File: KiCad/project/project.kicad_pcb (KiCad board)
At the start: 2 copper layers, 161 x 95.5 mm, 11 parts, among them U1 NUCLEO-L476RG

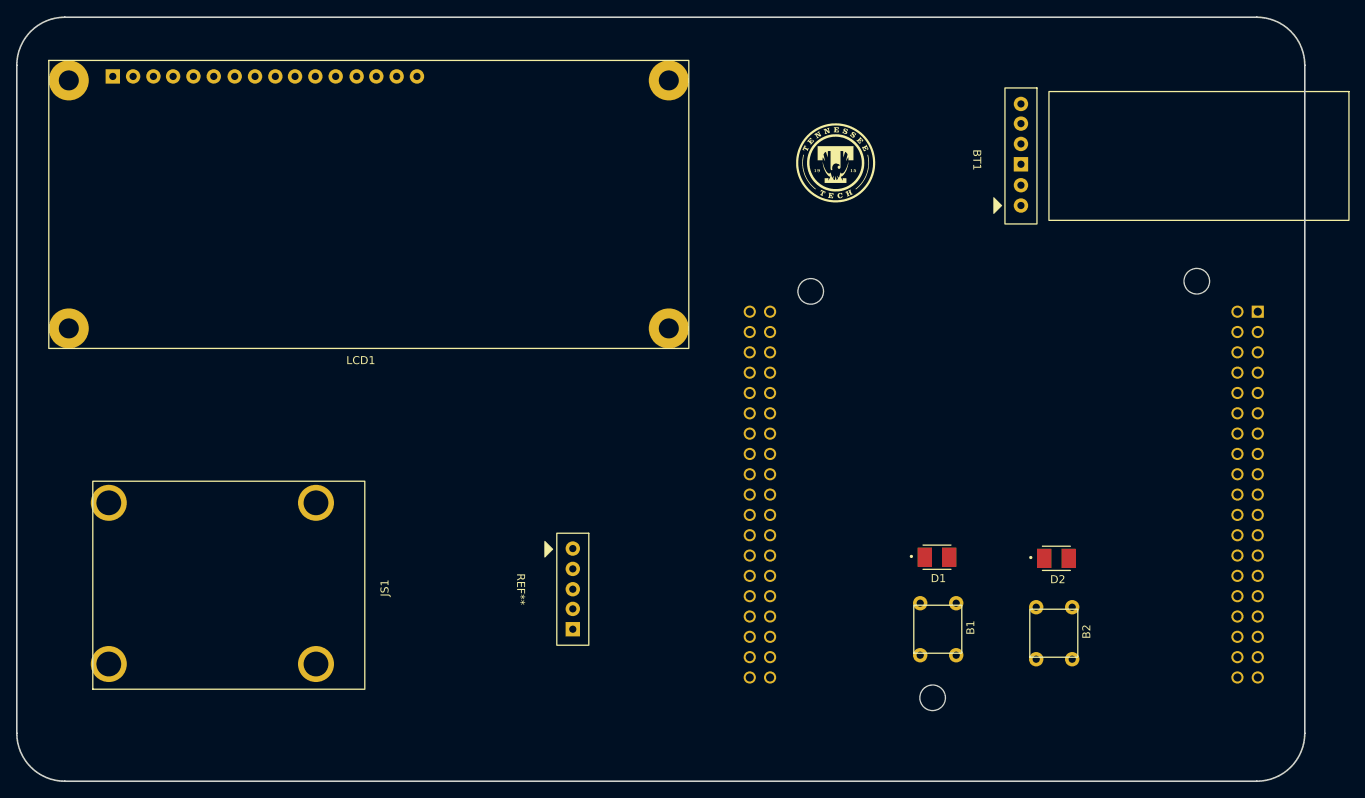
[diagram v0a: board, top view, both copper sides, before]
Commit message: Updated PCB schematic and pinout for the ioc file because it was funky
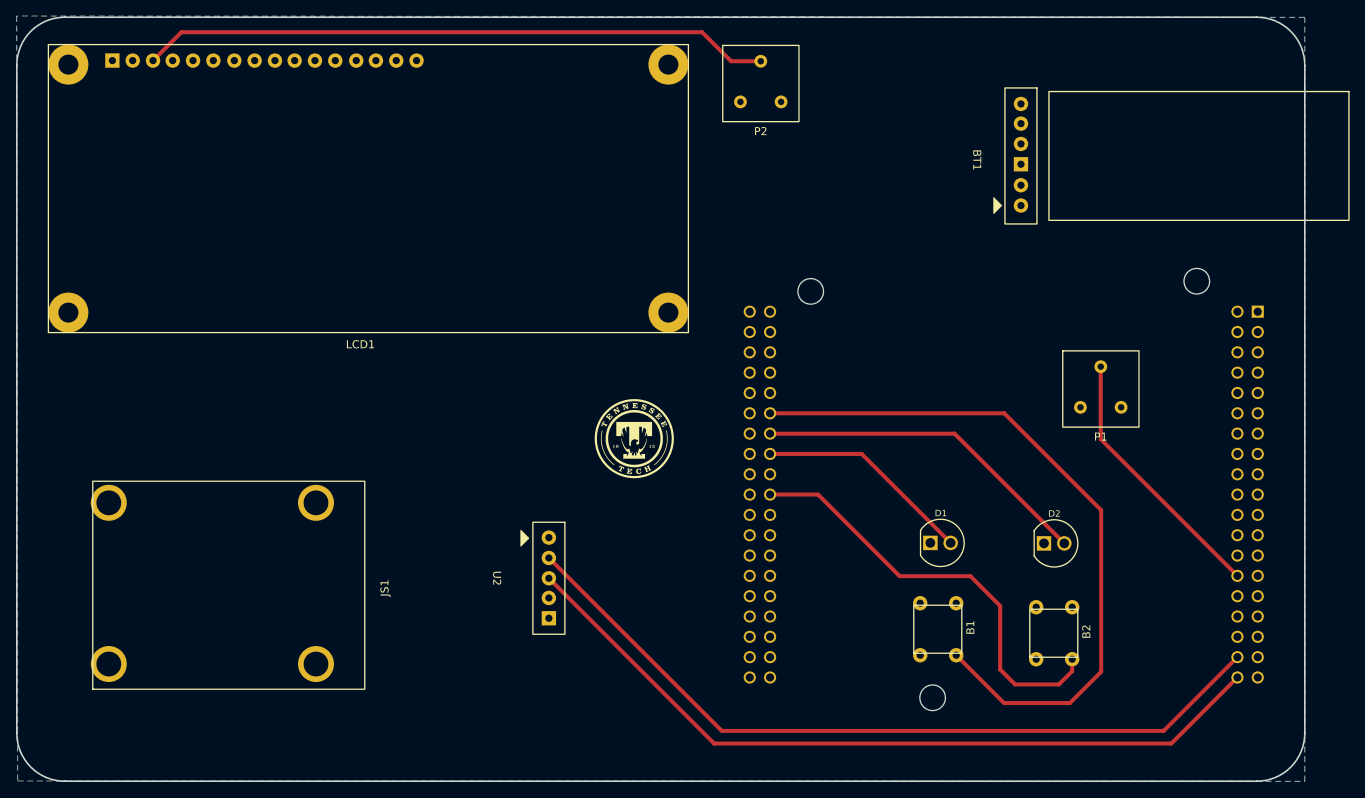
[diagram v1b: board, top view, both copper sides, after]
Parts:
- removed REF**: Joystick_Pins, Embedded_Footprints:Joystick_Pins
- added P1: ~, Embedded_Footprints:Potentiometer, F.Cu at (189.0, 114.5)
- added P2: ~, Embedded_Footprints:Potentiometer, F.Cu at (146.5, 76.3)
- added U2: ~, Embedded_Footprints:Joystick_Pins, F.Cu at (113.0, 131.6)
- D1, D2: footprint Embedded_Footprints:LED -> Embedded_Footprints:LED_THRU
- moved G*** 42.7 mm to (130.7, 114.2)
- moved D2 5.04 mm to (183.2, 127.3)
- moved D1 4.95 mm to (169.0, 127.2)
- moved LCD1 1.98 mm to (96.5, 102.9)
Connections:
- B1 pad 1: unconnected-(B1-Pad1) -> +5V
- B1 pad 2: unconnected-(B1-Pad2) -> /SD_BTN
- B1 pad 4: Net-(D1-A) -> Net-(B1-Pad4)
- B2 pad 1: unconnected-(B2-Pad1) -> +5V
- B2 pad 2: unconnected-(B2-Pad2) -> /MM_BTN
- B2 pad 4: Net-(D2-A) -> Net-(B2-Pad4)
- BT1 pad 1: unconnected-(BT1-EN-Pad1) -> /BT_EN
- BT1 pad 2: unconnected-(BT1-Vcc-Pad2) -> +5V
- BT1 pad 3: unconnected-(BT1-GND-Pad3) -> GND
- BT1 pad 4: unconnected-(BT1-TX-Pad4) -> /BT_TX
- BT1 pad 5: unconnected-(BT1-RX-Pad5) -> /BT_RX
- BT1 pad 6: unconnected-(BT1-State-Pad6) -> /BT_ST
- D1 pad 2: Net-(D1-A) -> /SD_LED
- D2 pad 2: Net-(D2-A) -> /MM_LED
- LCD1 pad 1: unconnected-(LCD1-GND-Pad1) -> GND
- LCD1 pad 10: unconnected-(LCD1-Data3-Pad10) -> /LCD_D3
- LCD1 pad 11: unconnected-(LCD1-Data4-Pad11) -> /LCD_D4
- LCD1 pad 12: unconnected-(LCD1-Data5-Pad12) -> /LCD_D5
- LCD1 pad 13: unconnected-(LCD1-Data6-Pad13) -> /LCD_D6
- LCD1 pad 14: unconnected-(LCD1-Data7-Pad14) -> /LCD_D7
- LCD1 pad 15: (no net) -> +5V
- LCD1 pad 16: (no net) -> GND
- LCD1 pad 2: unconnected-(LCD1-Vcc-Pad2) -> +5V
- LCD1 pad 3: unconnected-(LCD1-VE-Pad3) -> /LCD_Pot
- LCD1 pad 4: unconnected-(LCD1-RS-Pad4) -> /LCD_RS
- LCD1 pad 5: unconnected-(LCD1-R/W-Pad5) -> GND
- LCD1 pad 6: unconnected-(LCD1-EN-Pad6) -> /LCD_EN
- LCD1 pad 7: unconnected-(LCD1-Data0-Pad7) -> /LCD_D0
- LCD1 pad 8: unconnected-(LCD1-Data1-Pad8) -> /LCD_D1
- LCD1 pad 9: unconnected-(LCD1-Data2-Pad9) -> /LCD_D2
- U1 pad CN10_11: unconnected-(U1B-PA5-PadCN10_11) -> /SD_BTN
- U1 pad CN10_12: unconnected-(U1B-PA12-PadCN10_12) -> /LCD_D4
- U1 pad CN10_13: unconnected-(U1B-PA6-PadCN10_13) -> /MM_LED
- U1 pad CN10_14: unconnected-(U1B-PA11-PadCN10_14) -> /LCD_D5
- U1 pad CN10_15: unconnected-(U1B-PA7-PadCN10_15) -> /SD_LED
- U1 pad CN10_16: unconnected-(U1B-PB12-PadCN10_16) -> /LCD_D2
- U1 pad CN10_18: unconnected-(U1B-PB11-PadCN10_18) -> /LCD_D3
- U1 pad CN10_19: unconnected-(U1B-PC7-PadCN10_19) -> /MM_BTN
- U1 pad CN10_2: unconnected-(U1B-PC8-PadCN10_2) -> /LCD_D0
- U1 pad CN10_22: unconnected-(U1B-PB2-PadCN10_22) -> /LCD_D6
- U1 pad CN10_24: unconnected-(U1B-PB1-PadCN10_24) -> /LCD_D7
- U1 pad CN10_32: unconnected-(U1B-AGND-PadCN10_32) -> GND
- U1 pad CN10_35: unconnected-(U1B-PA2-PadCN10_35) -> /BT_TX
- U1 pad CN10_37: unconnected-(U1B-PA3-PadCN10_37) -> /BT_RX
- U1 pad CN10_4: unconnected-(U1B-PC6-PadCN10_4) -> /LCD_D1
- U1 pad CN10_9: unconnected-(U1B-GND_CN10_9-PadCN10_9) -> GND
- U1 pad CN7_1: unconnected-(U1A-PC10-PadCN7_1) -> /LCD_RS
- U1 pad CN7_16: unconnected-(U1A-+3V3-PadCN7_16) -> +3.3V
- U1 pad CN7_18: unconnected-(U1A-+5V-PadCN7_18) -> +5V
- U1 pad CN7_19: unconnected-(U1A-GND_CN7_19-PadCN7_19) -> GND
- U1 pad CN7_20: unconnected-(U1A-GND_CN7_20-PadCN7_20) -> GND
- U1 pad CN7_22: unconnected-(U1A-GND_CN7_22-PadCN7_22) -> GND
- U1 pad CN7_28: unconnected-(U1A-PA0-PadCN7_28) -> /Pot_Val
- U1 pad CN7_3: unconnected-(U1A-PC12-PadCN7_3) -> /LCD_EN
- U1 pad CN7_35: unconnected-(U1A-PC2-PadCN7_35) -> /BT_ST
- U1 pad CN7_36: unconnected-(U1A-PC1-PadCN7_36) -> /JS_Y
- U1 pad CN7_37: unconnected-(U1A-PC3-PadCN7_37) -> /BT_EN
- U1 pad CN7_38: unconnected-(U1A-PC0-PadCN7_38) -> /JS_X
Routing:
- net /JS_Y: track 0.00 -> 98.8 mm
- net /JS_X: track 0.00 -> 98.0 mm
- net /SD_BTN: track 0.00 -> 88.8 mm
- net /LCD_Pot: track 0.00 -> 78.9 mm
- net /MM_BTN: track 0.00 -> 54.4 mm
- net /MM_LED: track 0.00 -> 42.5 mm
- net /Pot_Val: track 0.00 -> 33.2 mm
- net /SD_LED: track 0.00 -> 27.2 mm
- added copper zone on B.Cu, net GND

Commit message: Update stuff :)
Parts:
- added H1: ~, Embedded_Footprints:OLED, F.Cu at (118.2, 107.2)
- added R1: R_US, Embedded_Footprints:RESC3216X65, F.Cu at (176.4, 138.2)
- added R2: R_US, Embedded_Footprints:RESC3216X65, F.Cu at (191.0, 138.1)
- moved G*** 41.9 mm to (170.6, 101.3)
- moved U2 37.5 mm to (77.4, 143.5), turned to 180 degrees
- moved JS1 25.6 mm to (77.2, 144.5), turned to 0 degrees
- moved B2 5.51 mm to (183.5, 141.9), turned to 0 degrees
- moved B1 5.37 mm to (169.8, 141.9), turned to 0 degrees
- moved D1 0.88 mm to (169.8, 127.0)
- moved D2 0.64 mm to (183.7, 127.0)
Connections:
- U1 pad CN10_11: /SD_BTN -> unconnected-(U1B-PA5-PadCN10_11)
- U1 pad CN10_14: /LCD_D5 -> /LCD_D3
- U1 pad CN10_17: unconnected-(U1B-PB6-PadCN10_17) -> /SD_BTN
- U1 pad CN10_18: /LCD_D3 -> /LCD_D1
- U1 pad CN10_2: /LCD_D0 -> /LCD_D7
- U1 pad CN10_22: /LCD_D6 -> /LCD_D0
- U1 pad CN10_24: /LCD_D7 -> /LCD_EN
- U1 pad CN10_26: unconnected-(U1B-PB15-PadCN10_26) -> /LCD_RS
- U1 pad CN10_28: unconnected-(U1B-PB14-PadCN10_28) -> /OLED_SDA
- U1 pad CN10_3: unconnected-(U1B-PB8-PadCN10_3) -> /BT_ST
- U1 pad CN10_30: unconnected-(U1B-PB13-PadCN10_30) -> /OLED_SCL
- U1 pad CN10_32: GND -> unconnected-(U1B-AGND-PadCN10_32)
- U1 pad CN10_35: /BT_TX -> unconnected-(U1B-PA2-PadCN10_35)
- U1 pad CN10_37: /BT_RX -> unconnected-(U1B-PA3-PadCN10_37)
- U1 pad CN10_4: /LCD_D1 -> /LCD_D6
- U1 pad CN10_5: unconnected-(U1B-PB9-PadCN10_5) -> /BT_EN
- U1 pad CN10_6: unconnected-(U1B-PC5-PadCN10_6) -> /LCD_D5
- U1 pad CN7_1: /LCD_RS -> unconnected-(U1A-PC10-PadCN7_1)
- U1 pad CN7_3: /LCD_EN -> /BT_TX
- U1 pad CN7_35: /BT_ST -> unconnected-(U1A-PC2-PadCN7_35)
- U1 pad CN7_37: /BT_EN -> unconnected-(U1A-PC3-PadCN7_37)
- U1 pad CN7_4: unconnected-(U1A-PD2-PadCN7_4) -> /BT_RX
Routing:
- net +5V: track 0.05 -> 385.4 mm
- net +3.3V: track 0.00 -> 119.6 mm, vias 0 -> 2
- net /LCD_RS: track 0.00 -> 97.8 mm
- net /LCD_EN: track 0.00 -> 92.9 mm
- net /LCD_D0: track 0.00 -> 89.3 mm
- net /LCD_D1: track 0.00 -> 84.7 mm
- net /LCD_D2: track 0.00 -> 81.1 mm
- net /LCD_D3: track 0.00 -> 76.2 mm
- net /LCD_D4: track 0.00 -> 72.6 mm
- net /LCD_D5: track 0.00 -> 66.9 mm
- net /LCD_D6: track 0.00 -> 63.2 mm
- net /BT_TX: track 0.00 -> 59.7 mm
- net /LCD_D7: track 0.00 -> 59.7 mm
- net /SD_BTN: track 88.8 -> 31.1 mm
- net /BT_RX: track 0.00 -> 55.5 mm
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
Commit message: Updated schematic to get ready to send out
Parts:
- moved G*** 1.01 mm to (61.7, 150.0)
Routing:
- net +5V: track 385.4 -> 412.4 mm
- net /Pot_Val: track 36.5 -> 35.0 mm
- net /BT_TX: track 59.7 -> 60.9 mm
- net +3.3V: track 119.6 -> 120.1 mm, vias 2 -> 1
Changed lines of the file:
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@@
 	(footprint "Graphics:TA_Logo"
 		(layer "B.Cu")
-		(at 61.91 151.01 180)
+		(at 61.7 150.02 180)
 		(property "Reference" "G***"
 			(at 0 0 180)
@@
 	)
 	(segment
+		(start 202.98 121.73)
+		(end 202.98 145.82)
+		(width 0.5)
+		(layer "F.Cu")
+		(net 2)
+	)
+	(segment
+		(start 76.88 153.6)
+		(end 74.94 151.66)
+		(width 0.5)
+		(layer "F.Cu")
+		(net 2)
+	)
+	(segment
 		(start 179.36 68.17)
 		(end 152.94951 68.17)
@@
 	)
 	(segment
-		(start 77.01 153.73)
-		(end 73.86 150.58)
-		(width 0.5)
-		(layer "F.Cu")
-		(net 2)
-	)
-	(segment
 		(start 149.037353 72.082157)
 		(end 147.267843 72.082157)
@@
 	)
 	(segment
+		(start 206.08 118.63)
+		(end 195.58 118.63)
+		(width 0.5)
+		(layer "F.Cu")
+		(net 2)
+	)
+	(segment
 		(start 152.94951 68.17)
 		(end 149.037353 72.082157)
@@
 	)
 	(segment
+		(start 74.94 151.66)
+		(end 74.94 150.48)
+		(width 0.5)
+		(layer "F.Cu")
+		(net 2)
+	)
+	(segment
 		(start 166.34 135.125)
 		(end 169.285 132.18)
@@
 	)
 	(segment
-		(start 202.39 146.41)
-		(end 195.07 153.73)
-		(width 0.5)
-		(layer "F.Cu")
-		(net 2)
-	)
-	(segment
 		(start 104.33 70.32)
 		(end 100.93 66.92)
@@
 	)
 	(segment
-		(start 200.12 118.63)
-		(end 191.537353 127.212647)
+		(start 202.98 145.82)
+		(end 195.2 153.6)
 		(width 0.5)
 		(layer "F.Cu")
@@
 	)
 	(segment
+		(start 195.58 118.63)
+		(end 191.537353 122.672647)
+		(width 0.5)
+		(layer "F.Cu")
+		(net 2)
+	)
+	(segment
+		(start 206.08 118.63)
+		(end 202.98 121.73)
+		(width 0.5)
+		(layer "F.Cu")
+		(net 2)
+	)
+	(segment
 		(start 191.537353 110.262157)
 		(end 191.537353 127.212647)
@@
 	)
 	(segment
-		(start 206.08 118.63)
-		(end 200.12 118.63)
-		(width 0.5)
-		(layer "F.Cu")
-		(net 2)
-	)
-	(segment
 		(start 191.537353 110.262157)
 		(end 191.537353 90.057353)
@@
 	)
 	(segment
-		(start 195.07 153.73)
-		(end 77.01 153.73)
+		(start 195.2 153.6)
+		(end 76.88 153.6)
 		(width 0.5)
 		(layer "F.Cu")
@@
 	)
 	(segment
+		(start 177.48 90.88)
+		(end 174.19 87.59)
+		(width 0.5)
+		(layer "B.Cu")
+		(net 9)
+	)
+	(segment
+		(start 208.47 90.88)
+		(end 177.48 90.88)
+		(width 0.5)
+		(layer "B.Cu")
+		(net 9)
+	)
+	(segment
 		(start 174.19 82.17)
 		(end 179.02 77.34)
@@
 	)
 	(segment
-		(start 211.49 96.64)
-		(end 205.73 90.88)
+		(start 211 100.26)
+		(end 211 93.41)
 		(width 0.5)
 		(layer "B.Cu")
@@
 	)
 	(segment
-		(start 211.49 99.77)
-		(end 211.49 96.64)
+		(start 211 93.41)
+		(end 208.47 90.88)
 		(width 0.5)
 		(layer "B.Cu")
@@
 	)
 	(segment
-		(start 177.48 90.88)
-		(end 174.19 87.59)
+		(start 208.62 100.85)
+		(end 210.41 100.85)
 		(width 0.5)
 		(layer "B.Cu")
@@
 	)
 	(segment
-		(start 205.73 90.88)
-		(end 177.48 90.88)
+		(start 210.41 100.85)
+		(end 211 100.26)
 		(width 0.5)
 		(layer "B.Cu")
@@
 		(start 174.19 87.59)
 		(end 174.19 82.17)
-		(width 0.5)
-		(layer "B.Cu")
-		(net 9)
-	)
-	(segment
-		(start 210.41 100.85)
-		(end 211.49 99.77)
-		(width 0.5)
-		(layer "B.Cu")
-		(net 9)
-	)
-	(segment
-		(start 208.62 100.85)
-		(end 210.41 100.85)
 		(width 0.5)
 		(layer "B.Cu")
@@
 	)
 	(segment
-		(start 202.71 122.25)
-		(end 202.71 135.4)
+		(start 186.21 151.9)
+		(end 136.53 151.9)
 		(width 0.5)
 		(layer "F.Cu")
@@
 	)
 	(segment
-		(start 136.59 151.96)
+		(start 200.22 137.89)
+		(end 186.21 151.9)
+		(width 0.5)
+		(layer "F.Cu")
+		(net 24)
+	)
+	(segment
+		(start 136.53 151.9)
 		(end 119.43 134.8)
 		(width 0.5)
@@
 	)
 	(segment
-		(start 202.71 116.62)
-		(end 202.71 116.64)
+		(start 200.22 121.91)
+		(end 200.22 137.89)
 		(width 0.5)
 		(layer "F.Cu")
 		(net 24)
 	)
-	(segment
-		(start 203.24 116.09)
-		(end 202.71 116.62)
-		(width 0.5)
-		(layer "F.Cu")
-		(net 24)
-	)
-	(segment
-		(start 202.71 135.4)
-		(end 186.15 151.96)
-		(width 0.5)
-		(layer "F.Cu")
-		(net 24)
-	)
-	(segment
-		(start 203.24 116.09)
-		(end 206.08 116.09)
-		(width 0.5)
-		(layer "F.Cu")
-		(net 24)
-	)
-	(segment
-		(start 186.15 151.96)
-		(end 136.59 151.96)
-		(width 0.5)
-		(layer "F.Cu")
-		(net 24)
-	)
 	(via
-		(at 202.71 122.25)
+		(at 200.22 121.91)
 		(size 0.6)
 		(drill 0.3)
@@
 		(net 24)
 	)
-	(via
-		(at 202.71 116.64)
-		(size 0.6)
-		(drill 0.3)
-		(layers "F.Cu" "B.Cu")
+	(segment
+		(start 202.33 116.09)
+		(end 206.08 116.09)
+		(width 0.5)
+		(layer "B.Cu")
 		(net 24)
 	)
 	(segment
-		(start 202.71 116.64)
-		(end 202.71 122.25)
+		(start 200.22 118.2)
+		(end 202.33 116.09)
 		(width 0.5)
 		(layer "B.Cu")
@@
 	)
 	(segment
-		(start 78.86 150.58)
+		(start 200.22 121.91)
+		(end 200.22 118.2)
+		(width 0.5)
+		(layer "B.Cu")
+		(net 24)
+	)
+	(segment
+		(start 79.94 151.66)
 		(end 81.1 152.82)
+		(width 0.5)
+		(layer "B.Cu")
+		(net 25)
+	)
+	(segment
+		(start 194.75 152.82)
+		(end 206.08 141.49)
 		(width 0.5)
 		(layer "B.Cu")
@@
 	)
 	(segment
-		(start 194.75 152.82)
-		(end 206.08 141.49)
+		(start 79.94 150.48)
+		(end 79.94 151.66)
 		(width 0.5)
 		(layer "B.Cu")
@@
 	)
 	(segment
-		(start 80.23 154.49)
-		(end 76.32 150.58)
+		(start 195.62 154.49)
+		(end 80.23 154.49)
 		(width 0.5)
 		(layer "B.Cu")
@@
 	)
 	(segment
-		(start 195.62 154.49)
-		(end 80.23 154.49)
+		(start 77.4 151.66)
+		(end 77.4 150.48)
 		(width 0.5)
 		(layer "B.Cu")
@@
 	)
 	(segment
-		(start 199.42 110)
-		(end 194.602157 105.182157)
+		(start 80.23 154.49)
+		(end 77.4 151.66)
+		(width 0.5)
+		(layer "B.Cu")
+		(net 26)
+	)
+	(segment
+		(start 206.08 131.33)
+		(end 195.35 120.6)
 		(width 0.5)
 		(layer "B.Cu")
@@
 	)
 	(segment
-		(start 199.42 124.67)
-		(end 199.42 110)
+		(start 195.35 108.47)
+		(end 192.062157 105.182157)
 		(width 0.5)
 		(layer "B.Cu")
@@
 	)
 	(segment
-		(start 206.08 131.33)
-		(end 199.42 124.67)
+		(start 192.062157 105.182157)
+		(end 188.997353 105.182157)
 		(width 0.5)
 		(layer "B.Cu")
@@
 	)
 	(segment
-		(start 194.602157 105.182157)
-		(end 188.997353 105.182157)
-		(width 0.5)
-		(layer "B.Cu")
+		(start 195.35 120.6)
+		(end 195.35 108.47)
+		(width 0.5)
+		(layer "B.Cu")

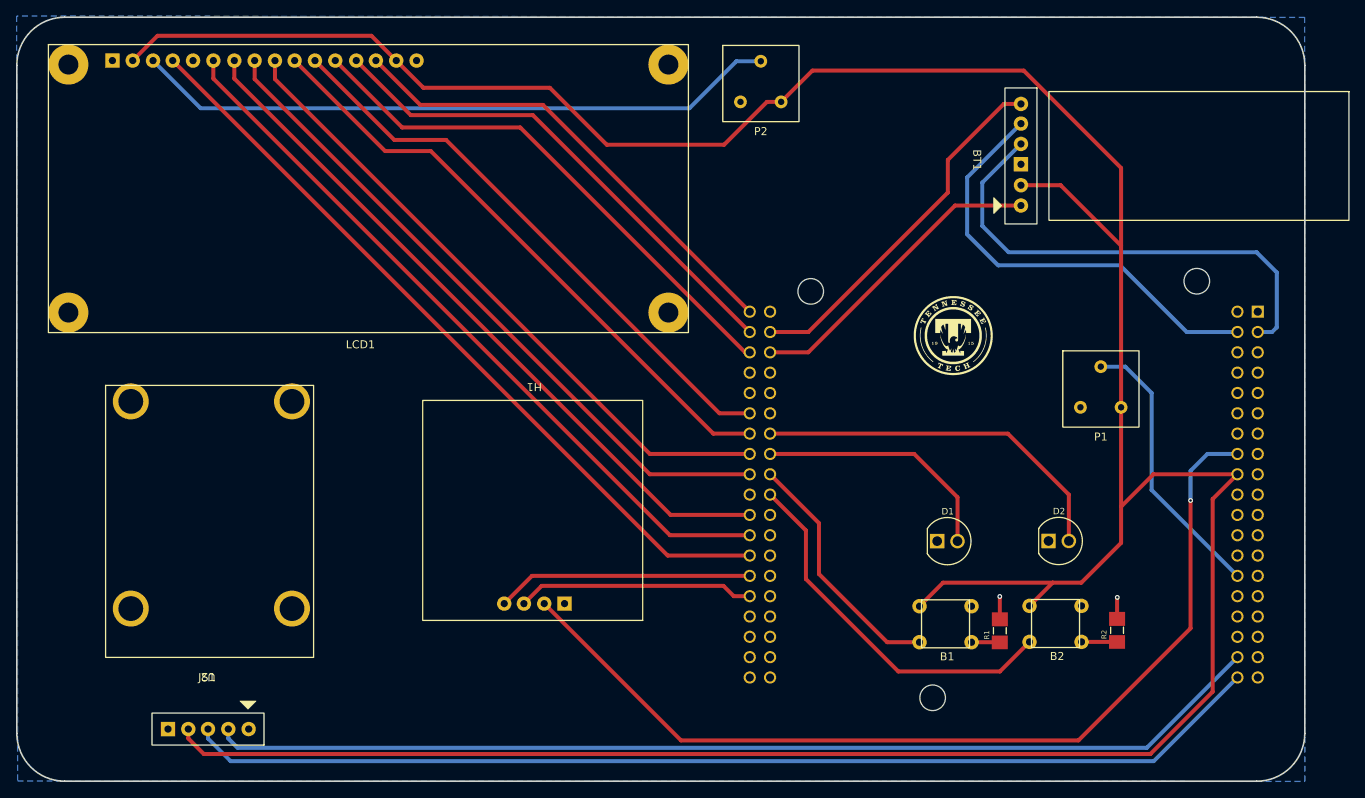
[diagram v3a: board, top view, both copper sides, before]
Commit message: Updated PCB for parallel capacitors
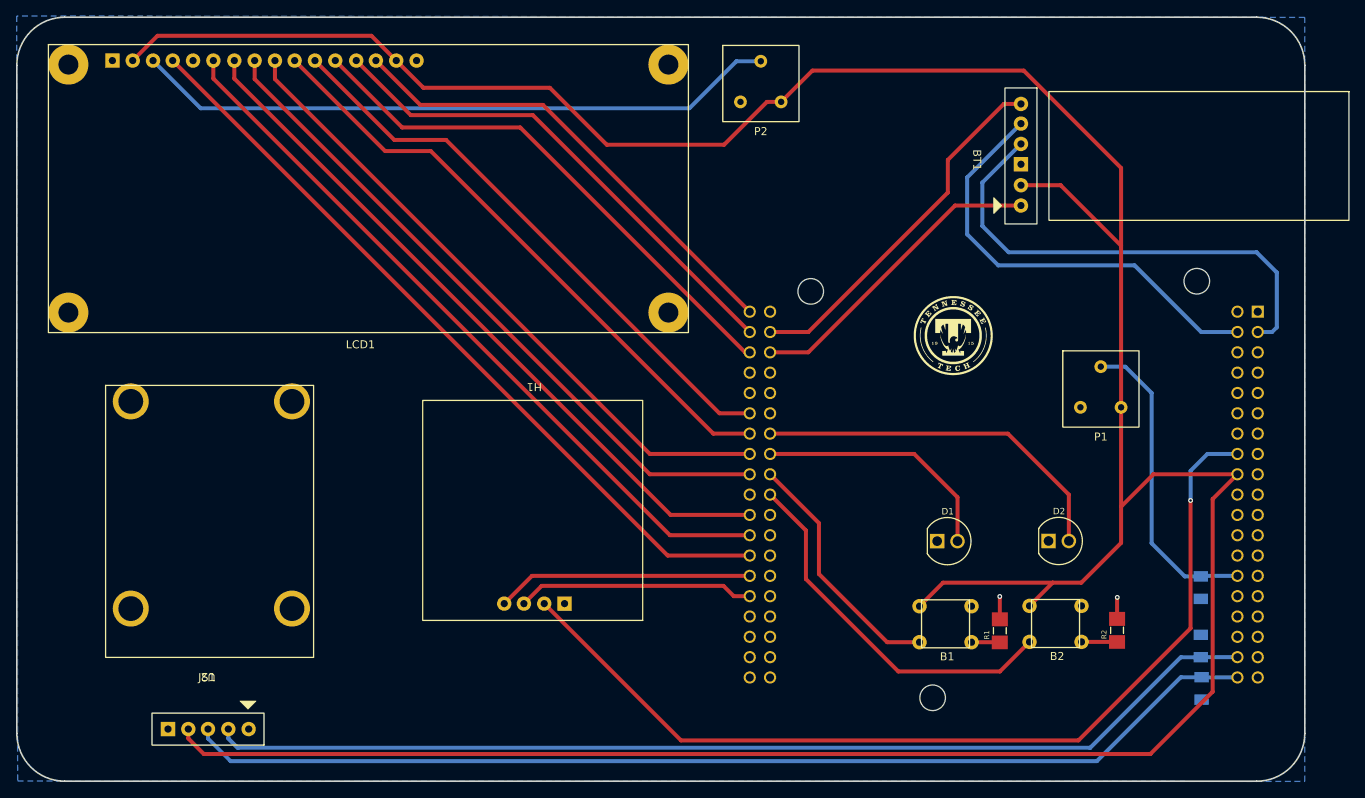
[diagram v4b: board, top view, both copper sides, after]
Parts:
- added C1: 10nF, Embedded_Footprints:CAPC340180_88N_KEM, B.Cu at (201.5, 132.8)
- added C2: 10nF, Embedded_Footprints:CAPC340180_88N_KEM, B.Cu at (201.6, 145.4)
- added C3: 10nF, Embedded_Footprints:CAPC340180_88N_KEM, B.Cu at (201.5, 140.1)
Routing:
- net /Pot_Val: track 35.0 -> 38.9 mm
